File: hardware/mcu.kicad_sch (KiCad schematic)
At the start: 43 parts, among them J10 SM03B-SRSS-TB, J9 USB_C_Receptacle_USB2.0_14P, SW2 SW_BOOT, SW3 SW_RESET, U10 W25Q128JVS, U7 NCP1117-3.3_SOT223, U8 RP2350A-QFN60, U9 W25Q128JVS, Y1 ABM8-272-T3

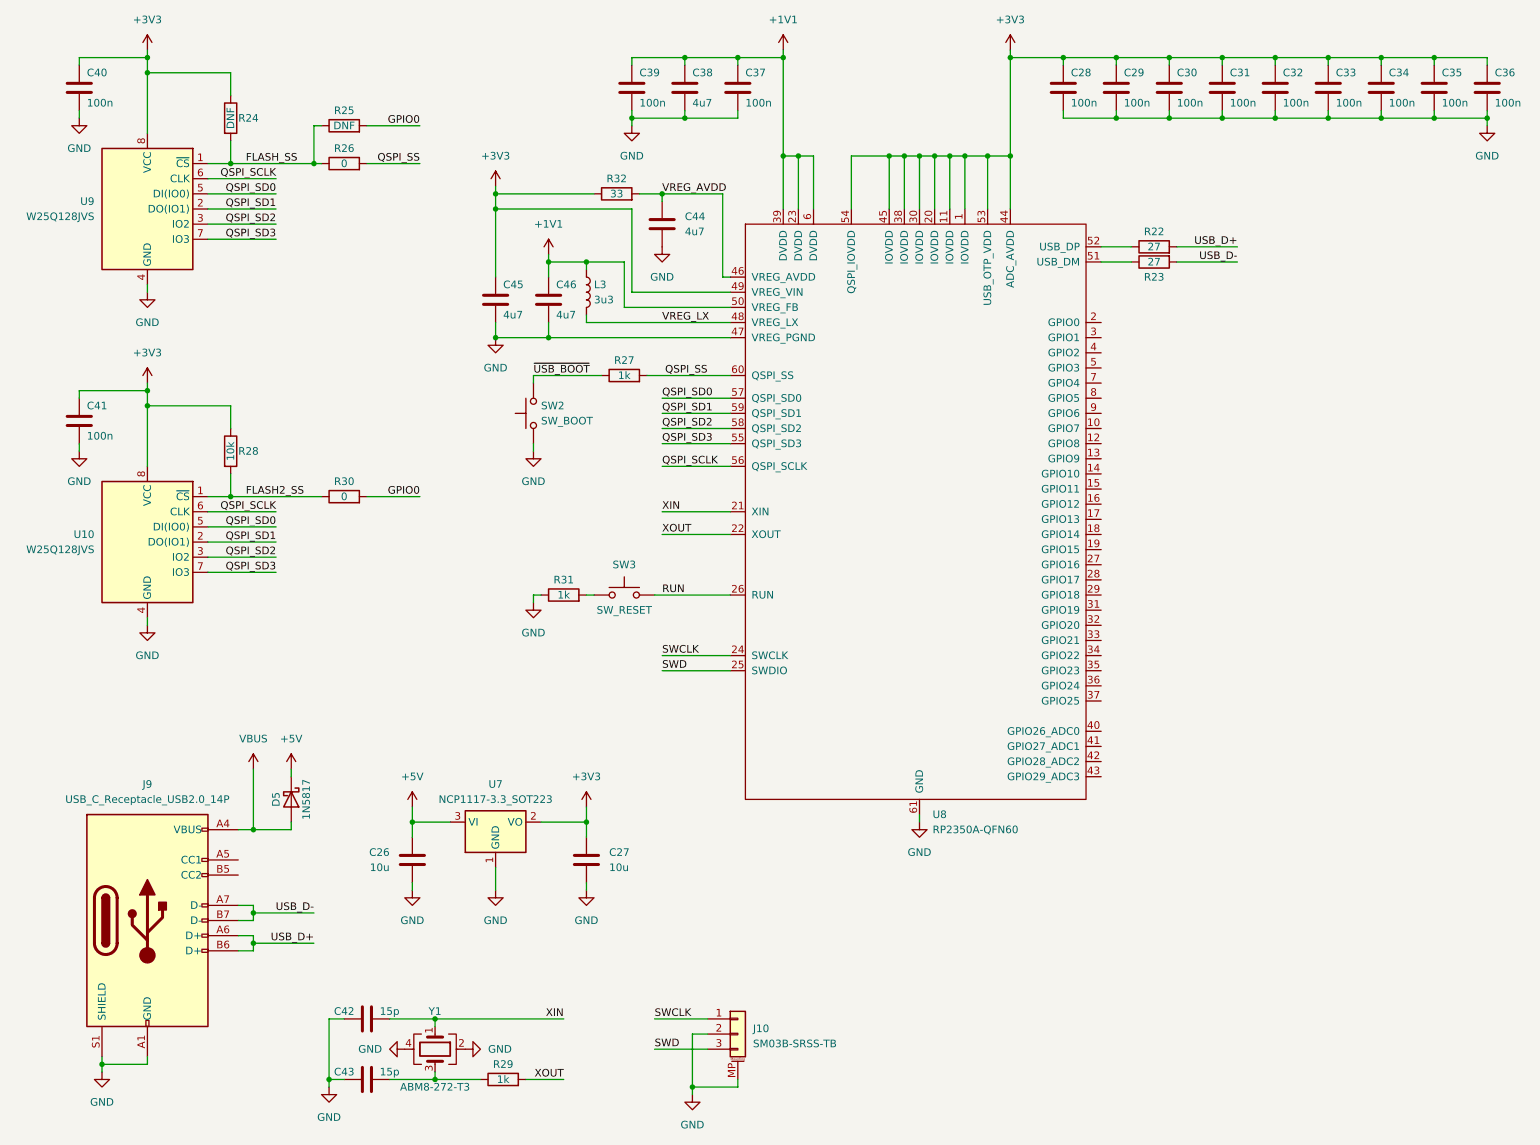
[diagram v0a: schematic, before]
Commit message: Schematic revision completed
New codec, TLV320AIC3104. Improved power isolation. More control inputs. Modular design.
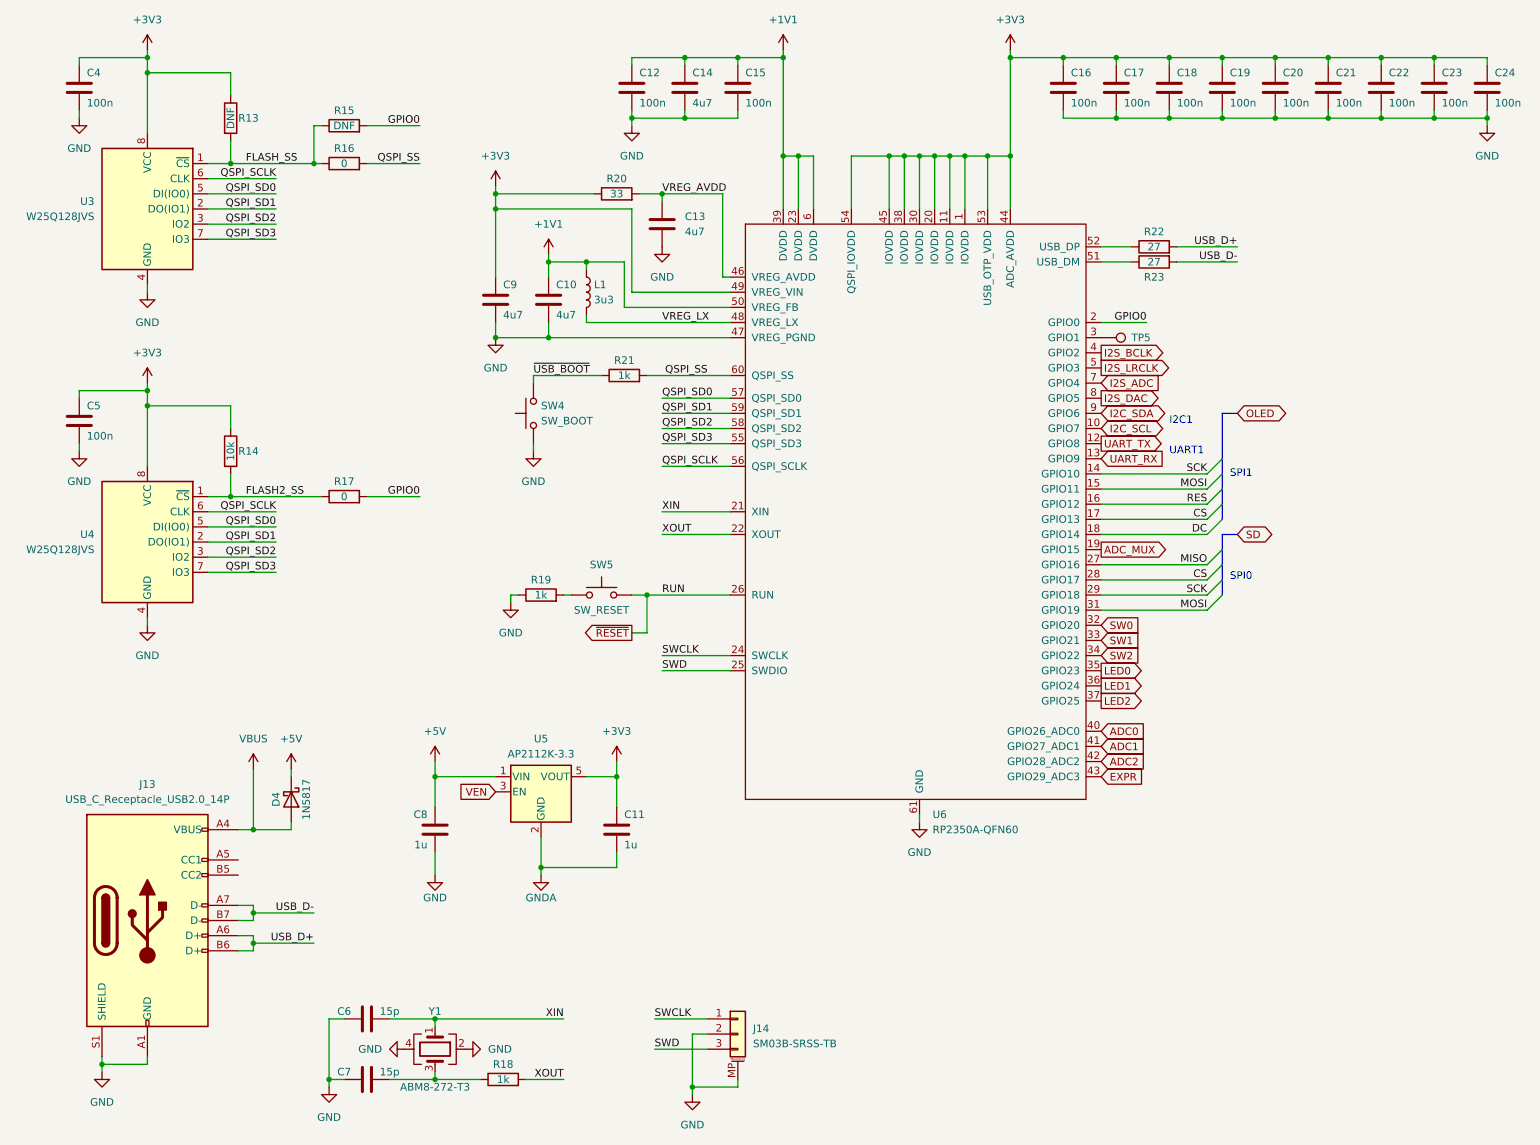
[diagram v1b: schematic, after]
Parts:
- removed C26, C27: 10u, symbol Device:C
- removed U7: NCP1117-3.3_SOT223, Package_TO_SOT_SMD:SOT-223-3_TabPin2, symbol Regulator_Linear:NCP1117-3.3_SOT223
- added C11, C8: 1u, symbol Device:C
- added TP5: TestPoint, symbol Connector:TestPoint
- added U5: AP2112K-3.3, Package_TO_SOT_SMD:SOT-23-5, symbol Regulator_Linear:AP2112K-3.3
- renumbered C46 to C10, C39 to C12, C44 to C13, C38 to C14, C37 to C15, C28 to C16, C29 to C17, C30 to C18, C31 to C19, C32 to C20, C33 to C21, C34 to C22, C35 to C23, C36 to C24, C40 to C4, C41 to C5, C42 to C6, C43 to C7, C45 to C9, D5 to D4, J9 to J13, J10 to J14, L3 to L1, R24 to R13, R28 to R14, R25 to R15, R26 to R16, R30 to R17, R29 to R18, R31 to R19, R32 to R20, R27 to R21, SW2 to SW4, SW3 to SW5, U9 to U3, U10 to U4, U8 to U6
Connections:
- net +3V3: now also C11.1, U5.5 (VOUT)
- net +5V: now also C8.1, U5.1 (VIN)
- net GND: now also C8.2
- net GPIO0: now also U6.2 (GPIO0)
- net I2C_SCL: now reaches U6.10 (GPIO7)
- net UART_TX: now reaches U6.12 (GPIO8)
- net UART_RX: now reaches U6.13 (GPIO9)
- net SCK: now reaches U6.14 (GPIO10)
- net SCK: now also U6.29 (GPIO18)
- net MOSI: now reaches U6.15 (GPIO11)
- net MOSI: now also U6.31 (GPIO19)
- net RES: now reaches U6.16 (GPIO12)
- net CS: now reaches U6.17 (GPIO13)
- net CS: now also U6.28 (GPIO17)
- net DC: now reaches U6.18 (GPIO14)
- net ADC_MUX: now reaches U6.19 (GPIO15)
- net MISO: now reaches U6.27 (GPIO16)
- net at U6.3 (GPIO1): now also TP5.1
- net SW0: now reaches U6.32 (GPIO20)
- net SW1: now reaches U6.33 (GPIO21)
- net SW2: now reaches U6.34 (GPIO22)
- net LED0: now reaches U6.35 (GPIO23)
- net LED1: now reaches U6.36 (GPIO24)
- net LED2: now reaches U6.37 (GPIO25)
- net I2S_BCLK: now reaches U6.4 (GPIO2)
- net ADC0: now reaches U6.40 (GPIO26_ADC0)
- net ADC1: now reaches U6.41 (GPIO27_ADC1)
- net ADC2: now reaches U6.42 (GPIO28_ADC2)
- net EXPR: now reaches U6.43 (GPIO29_ADC3)
- net I2S_LRCLK: now reaches U6.5 (GPIO3)
- net I2S_ADC: now reaches U6.7 (GPIO4)
- net I2S_DAC: now reaches U6.8 (GPIO5)
- net I2C_SDA: now reaches U6.9 (GPIO6)
- net RUN renamed ~{RESET}
- new net GNDA: C11.2, U5.2 (GND)
- new net VEN: U5.3 (EN)
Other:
- note added: "I2C1"
- note added: "SPI0"
- note added: "SPI1"
- note added: "UART1"
- moved on the sheet: R19, SW5

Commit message: Reset references and remove THT footprint assignments.
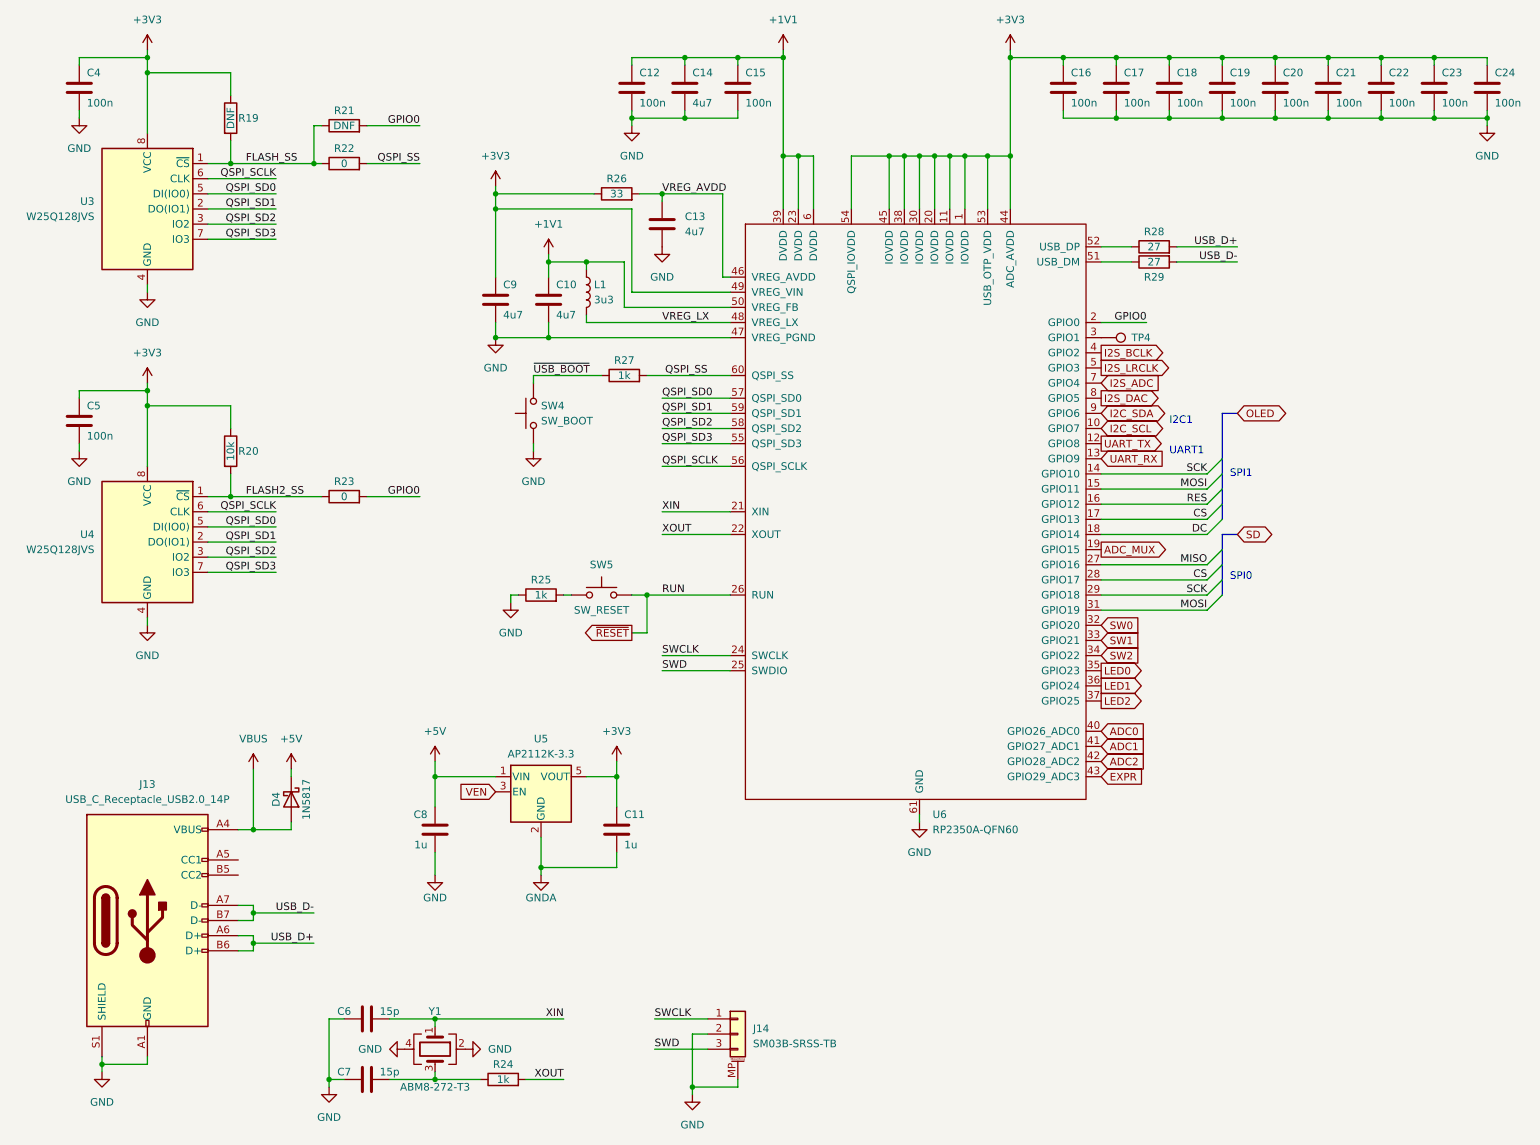
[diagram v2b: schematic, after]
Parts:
- D4: footprint Diode_THT:D_DO-41_SOD81_P2.54mm_Vertical_AnodeUp -> (none)
- U3, U4: footprint Package_SO:SOIC-8_5.23x5.23mm_P1.27mm -> Package_SO:SOIC-8_5.3x5.3mm_P1.27mm
- U6: footprint (none) -> Package_DFN_QFN:QFN-60-1EP_7x7mm_P0.4mm_EP3.4x3.4mm
- renumbered R13 to R19, R14 to R20, R15 to R21, R16 to R22, R17 to R23, R18 to R24, R19 to R25, R20 to R26, R21 to R27, R22 to R28, R23 to R29, TP5 to TP4
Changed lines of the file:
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@@
 		(on_board yes)
 		(dnp no)
-		(property "Reference" "R17"
+		(property "Reference" "R23"
 			(at 67.31 92.71 90)
 			(effects
@@
 			(project "Zero-Stomp"
 				(path "/8c8d5801-9c58-4283-98ac-c6a8e7250e15/18032a8d-c86f-4e94-b2bf-e3bf4b84450f"
-					(reference "R17")
+					(reference "R23")
 					(unit 1)
 				)
@@
 		(on_board yes)
 		(dnp no)
-		(property "Reference" "R20"
+		(property "Reference" "R26"
 			(at 113.03 41.91 90)
 			(effects
@@
 			(project "Zero-Stomp"
 				(path "/8c8d5801-9c58-4283-98ac-c6a8e7250e15/18032a8d-c86f-4e94-b2bf-e3bf4b84450f"
-					(reference "R20")
+					(reference "R26")
 					(unit 1)
 				)
@@
 		(on_board yes)
 		(dnp no)
-		(property "Reference" "R19"
+		(property "Reference" "R25"
 			(at 100.33 109.22 90)
 			(effects
@@
 			(project "Zero-Stomp"
 				(path "/8c8d5801-9c58-4283-98ac-c6a8e7250e15/18032a8d-c86f-4e94-b2bf-e3bf4b84450f"
-					(reference "R19")
+					(reference "R25")
 					(unit 1)
 				)
@@
 		(on_board yes)
 		(dnp no)
-		(property "Reference" "R14"
+		(property "Reference" "R20"
 			(at 49.53 87.63 0)
 			(effects
@@
 			(project "Zero-Stomp"
 				(path "/8c8d5801-9c58-4283-98ac-c6a8e7250e15/18032a8d-c86f-4e94-b2bf-e3bf4b84450f"
-					(reference "R14")
+					(reference "R20")
 					(unit 1)
 				)
@@
 		(on_board yes)
 		(dnp no)
-		(property "Reference" "R15"
+		(property "Reference" "R21"
 			(at 67.31 30.48 90)
 			(effects
@@
 			(project "Zero-Stomp"
 				(path "/8c8d5801-9c58-4283-98ac-c6a8e7250e15/18032a8d-c86f-4e94-b2bf-e3bf4b84450f"
-					(reference "R15")
+					(reference "R21")
 					(unit 1)
 				)
@@
 			)
 		)
-		(property "Footprint" ""
+		(property "Footprint" "Package_DFN_QFN:QFN-60-1EP_7x7mm_P0.4mm_EP3.4x3.4mm"
 			(at 152.4 76.2 0)
 			(effects
@@
 			)
 		)
-		(property "Footprint" "Package_SO:SOIC-8_5.23x5.23mm_P1.27mm"
+		(property "Footprint" "Package_SO:SOIC-8_5.3x5.3mm_P1.27mm"
 			(at 34.29 24.13 0)
 			(effects
@@
 		(on_board yes)
 		(dnp no)
-		(property "Reference" "R22"
+		(property "Reference" "R28"
 			(at 203.2 50.8 90)
 			(effects
@@
 			(project "Zero-Stomp"
 				(path "/8c8d5801-9c58-4283-98ac-c6a8e7250e15/18032a8d-c86f-4e94-b2bf-e3bf4b84450f"
-					(reference "R22")
+					(reference "R28")
 					(unit 1)
 				)
@@
 			)
 		)
-		(property "Footprint" "Diode_THT:D_DO-41_SOD81_P2.54mm_Vertical_AnodeUp"
+		(property "Footprint" ""
 			(at 53.975 146.05 0)
 			(effects
@@
 			)
 		)
-		(property "Footprint" "Package_SO:SOIC-8_5.23x5.23mm_P1.27mm"
+		(property "Footprint" "Package_SO:SOIC-8_5.3x5.3mm_P1.27mm"
 			(at 34.29 80.01 0)
 			(effects
@@
 		(on_board yes)
 		(dnp no)
-		(property "Reference" "R21"
+		(property "Reference" "R27"
 			(at 114.3 72.39 90)
 			(effects
@@
 			(project "Zero-Stomp"
 				(path "/8c8d5801-9c58-4283-98ac-c6a8e7250e15/18032a8d-c86f-4e94-b2bf-e3bf4b84450f"
-					(reference "R21")
+					(reference "R27")
 					(unit 1)
 				)
@@
 		(on_board yes)
 		(dnp no)
-		(property "Reference" "R13"
+		(property "Reference" "R19"
 			(at 49.53 31.75 0)
 			(effects
@@
 			(project "Zero-Stomp"
 				(path "/8c8d5801-9c58-4283-98ac-c6a8e7250e15/18032a8d-c86f-4e94-b2bf-e3bf4b84450f"
-					(reference "R13")
+					(reference "R19")
 					(unit 1)
 				)
@@
 		(on_board yes)
 		(dnp no)
-		(property "Reference" "TP5"
+		(property "Reference" "TP4"
 			(at 199.39 68.58 90)
 			(effects
@@
 			(project "Zero-Stomp"
 				(path "/8c8d5801-9c58-4283-98ac-c6a8e7250e15/18032a8d-c86f-4e94-b2bf-e3bf4b84450f"
-					(reference "TP5")
+					(reference "TP4")
 					(unit 1)
 				)
@@
 		(on_board yes)
 		(dnp no)
-		(property "Reference" "R23"
+		(property "Reference" "R29"
 			(at 203.2 58.42 90)
 			(effects
@@
 			(project "Zero-Stomp"
 				(path "/8c8d5801-9c58-4283-98ac-c6a8e7250e15/18032a8d-c86f-4e94-b2bf-e3bf4b84450f"
-					(reference "R23")
+					(reference "R29")
 					(unit 1)
 				)
@@
 		(on_board yes)
 		(dnp no)
-		(property "Reference" "R16"
+		(property "Reference" "R22"
 			(at 67.31 36.83 90)
 			(effects
@@
 			(project "Zero-Stomp"
 				(path "/8c8d5801-9c58-4283-98ac-c6a8e7250e15/18032a8d-c86f-4e94-b2bf-e3bf4b84450f"
-					(reference "R16")
+					(reference "R22")
 					(unit 1)
 				)
@@
 		(on_board yes)
 		(dnp no)
-		(property "Reference" "R18"
+		(property "Reference" "R24"
 			(at 93.98 190.5 90)
 			(effects
@@
 			(project "Zero-Stomp"
 				(path "/8c8d5801-9c58-4283-98ac-c6a8e7250e15/18032a8d-c86f-4e94-b2bf-e3bf4b84450f"
-					(reference "R18")
+					(reference "R24")
 					(unit 1)
 				)

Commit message: Rename 100n to 0u1
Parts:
- C12, C15, C16, C17, C18, C19, C20, C21, C22, C23, C24, C4, C5: value 100n -> 0u1
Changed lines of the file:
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@@
 			)
 		)
-		(property "Value" "100n"
+		(property "Value" "0u1"
 			(at 233.68 29.21 0)
 			(effects
@@
 			)
 		)
-		(property "Value" "100n"
+		(property "Value" "0u1"
 			(at 224.79 29.21 0)
 			(effects
@@
 			)
 		)
-		(property "Value" "100n"
+		(property "Value" "0u1"
 			(at 251.46 29.21 0)
 			(effects
@@
 			)
 		)
-		(property "Value" "100n"
+		(property "Value" "0u1"
 			(at 24.13 29.21 0)
 			(effects
@@
 			)
 		)
-		(property "Value" "100n"
+		(property "Value" "0u1"
 			(at 242.57 29.21 0)
 			(effects
@@
 			)
 		)
-		(property "Value" "100n"
+		(property "Value" "0u1"
 			(at 189.23 29.21 0)
 			(effects
@@
 			)
 		)
-		(property "Value" "100n"
+		(property "Value" "0u1"
 			(at 215.9 29.21 0)
 			(effects
@@
 			)
 		)
-		(property "Value" "100n"
+		(property "Value" "0u1"
 			(at 134.62 29.21 0)
 			(effects
@@
 			)
 		)
-		(property "Value" "100n"
+		(property "Value" "0u1"
 			(at 116.84 29.21 0)
 			(effects
@@
 			)
 		)
-		(property "Value" "100n"
+		(property "Value" "0u1"
 			(at 260.35 29.21 0)
 			(effects
@@
 			)
 		)
-		(property "Value" "100n"
+		(property "Value" "0u1"
 			(at 24.13 85.09 0)
 			(effects
@@
 			)
 		)
-		(property "Value" "100n"
+		(property "Value" "0u1"
 			(at 198.12 29.21 0)
 			(effects
@@
 			)
 		)
-		(property "Value" "100n"
+		(property "Value" "0u1"
 			(at 207.01 29.21 0)
 			(effects
